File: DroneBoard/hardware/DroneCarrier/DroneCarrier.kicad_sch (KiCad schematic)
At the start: 0 parts

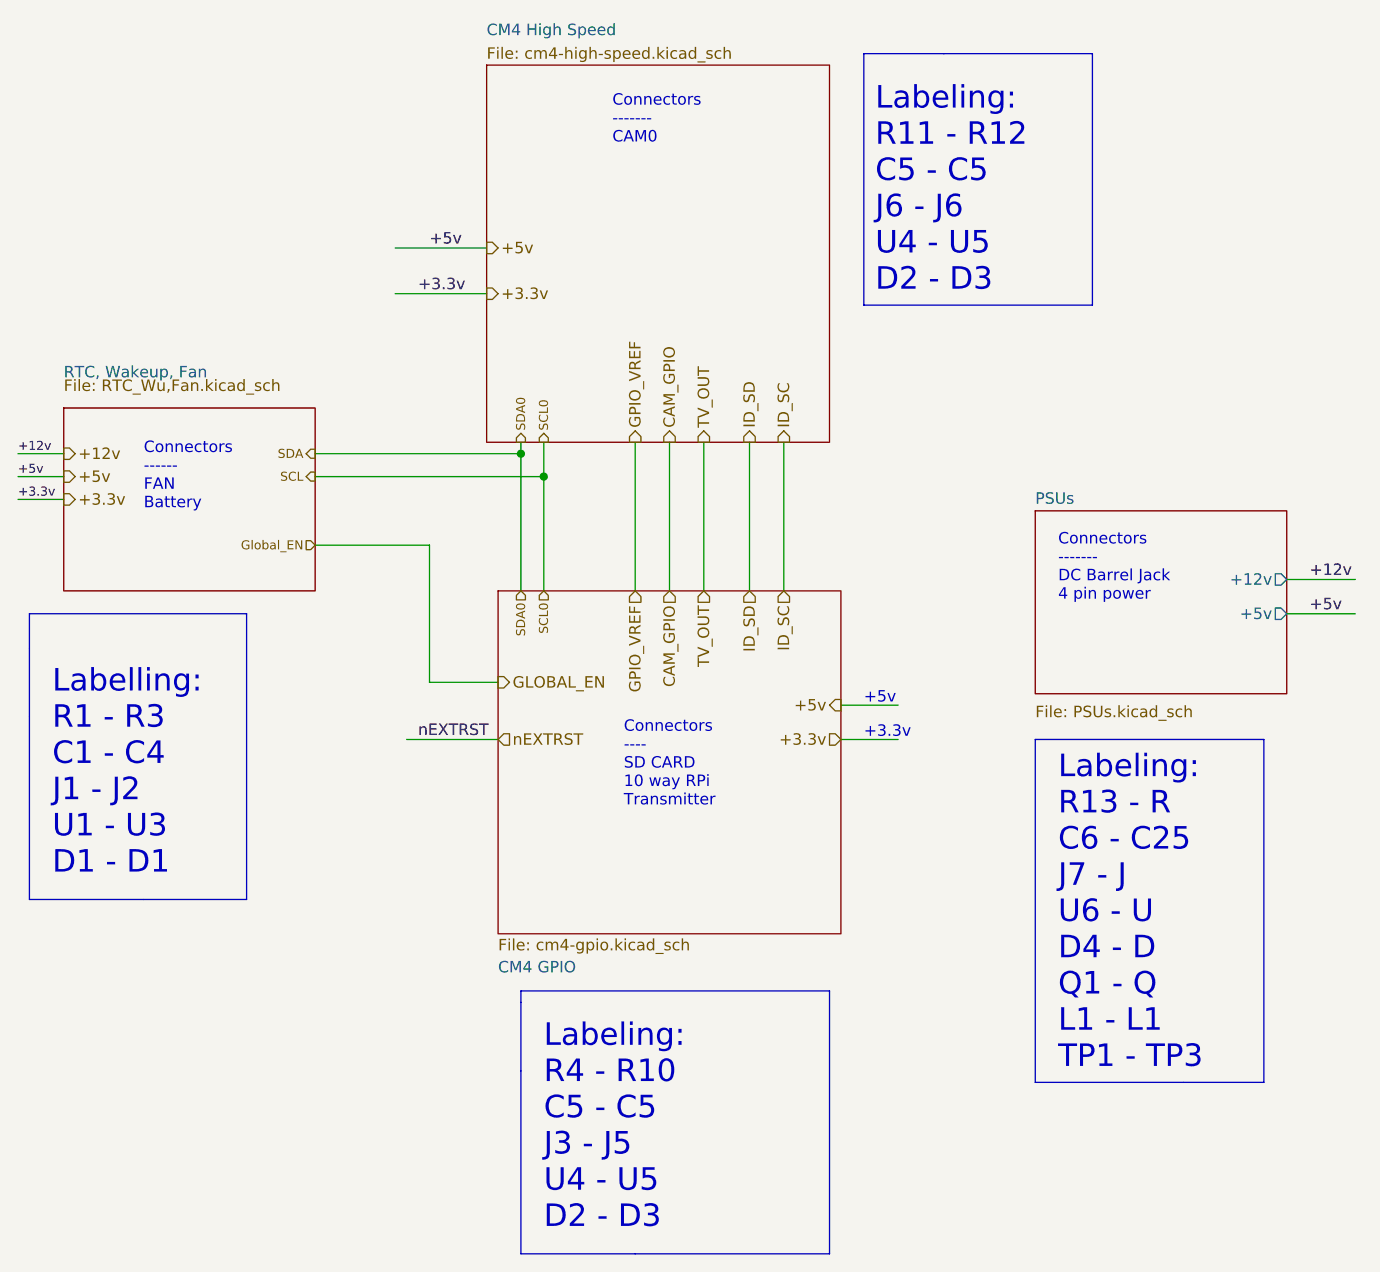
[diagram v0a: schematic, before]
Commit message: Labelling needs to be compared to the RPi CM4
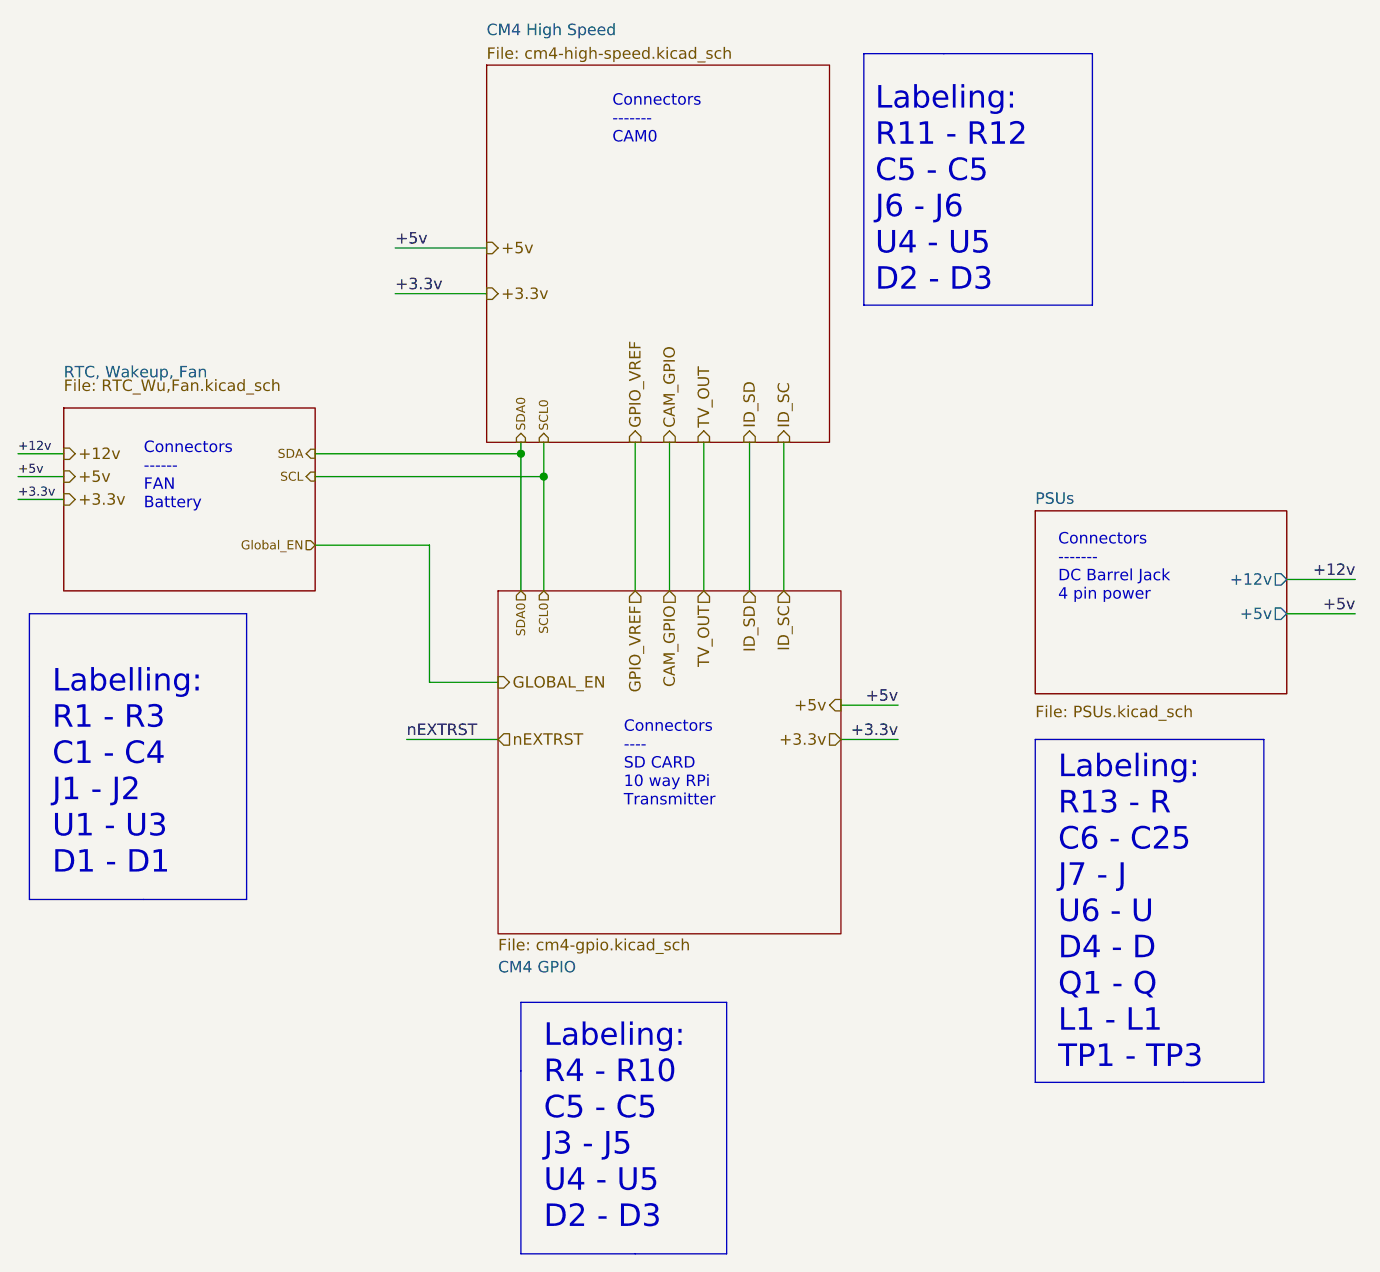
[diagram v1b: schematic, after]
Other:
- note removed: "+3.3v"
- note removed: "+5v"

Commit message: Add files via upload
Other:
- note added: "Connectors ------- DC Barrel Jack"
- note added: "Labeling: J7 - J7"
- note removed: "Connectors ------- DC Barrel Jack 4 pin power"
- note removed: "Labeling: R13 - R C6 - C25 J7 - J U6 - U D4 - D Q1 - Q L1 - L1 TP1 - TP3"
